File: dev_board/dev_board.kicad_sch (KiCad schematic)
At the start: 3 parts, among them P1 USB_C_Plug_USB2.0, U2 ATmega32L-8A

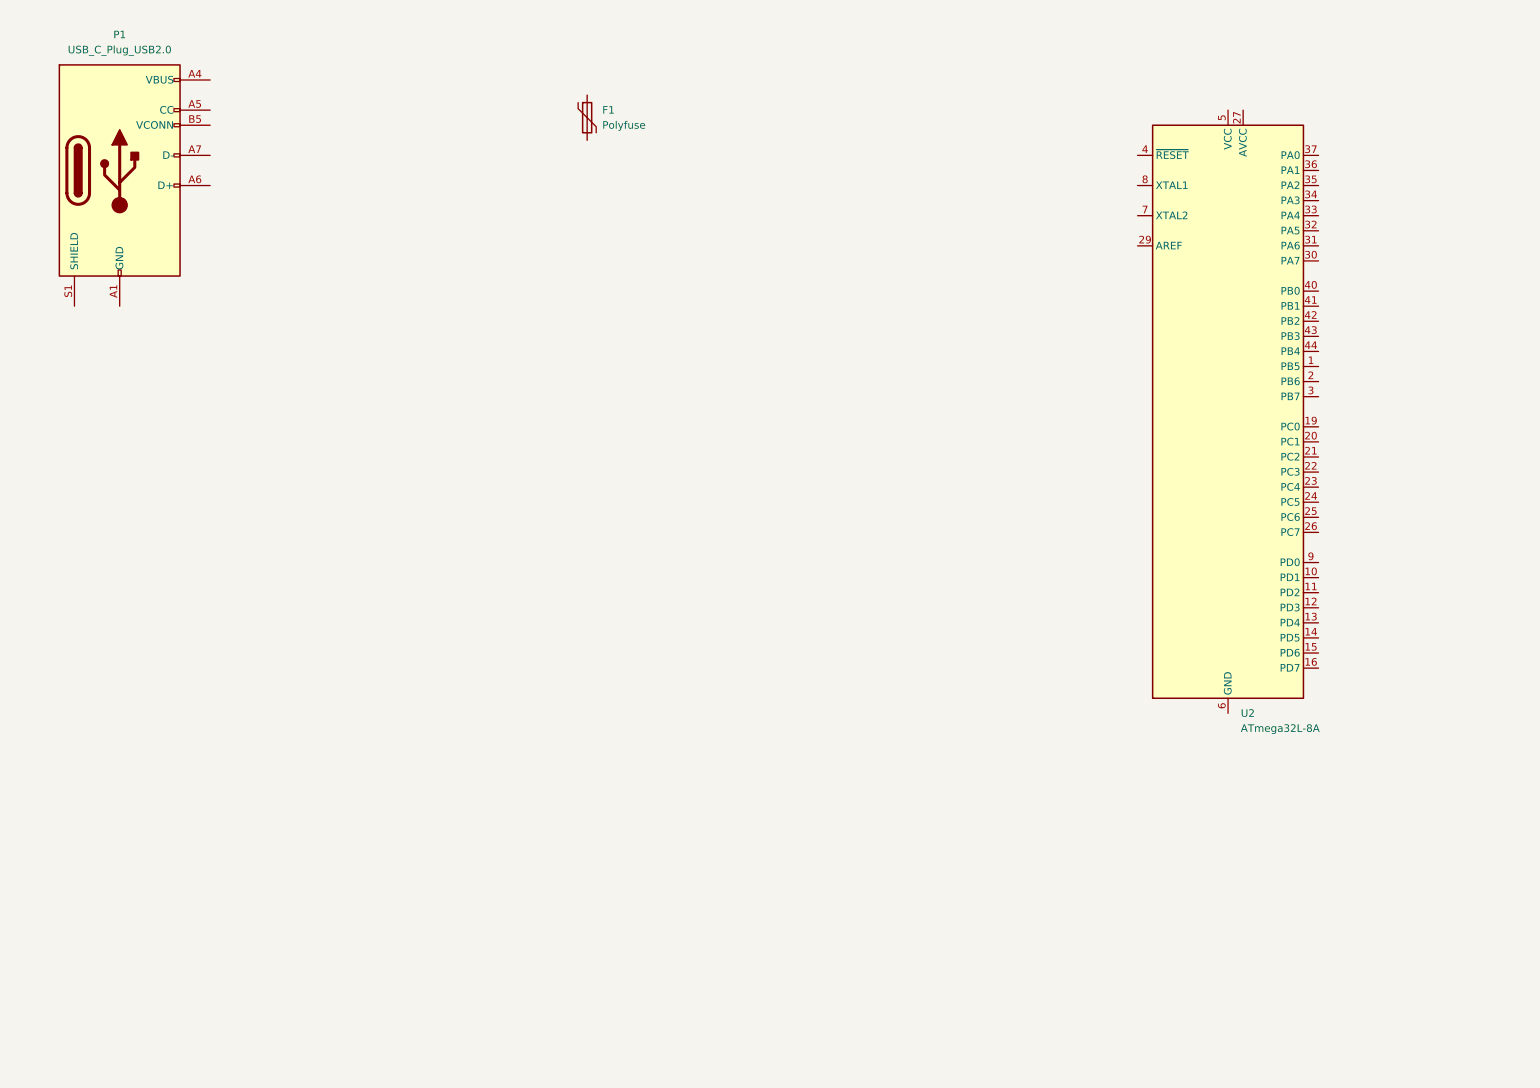
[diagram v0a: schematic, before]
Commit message: schematic autosave issue
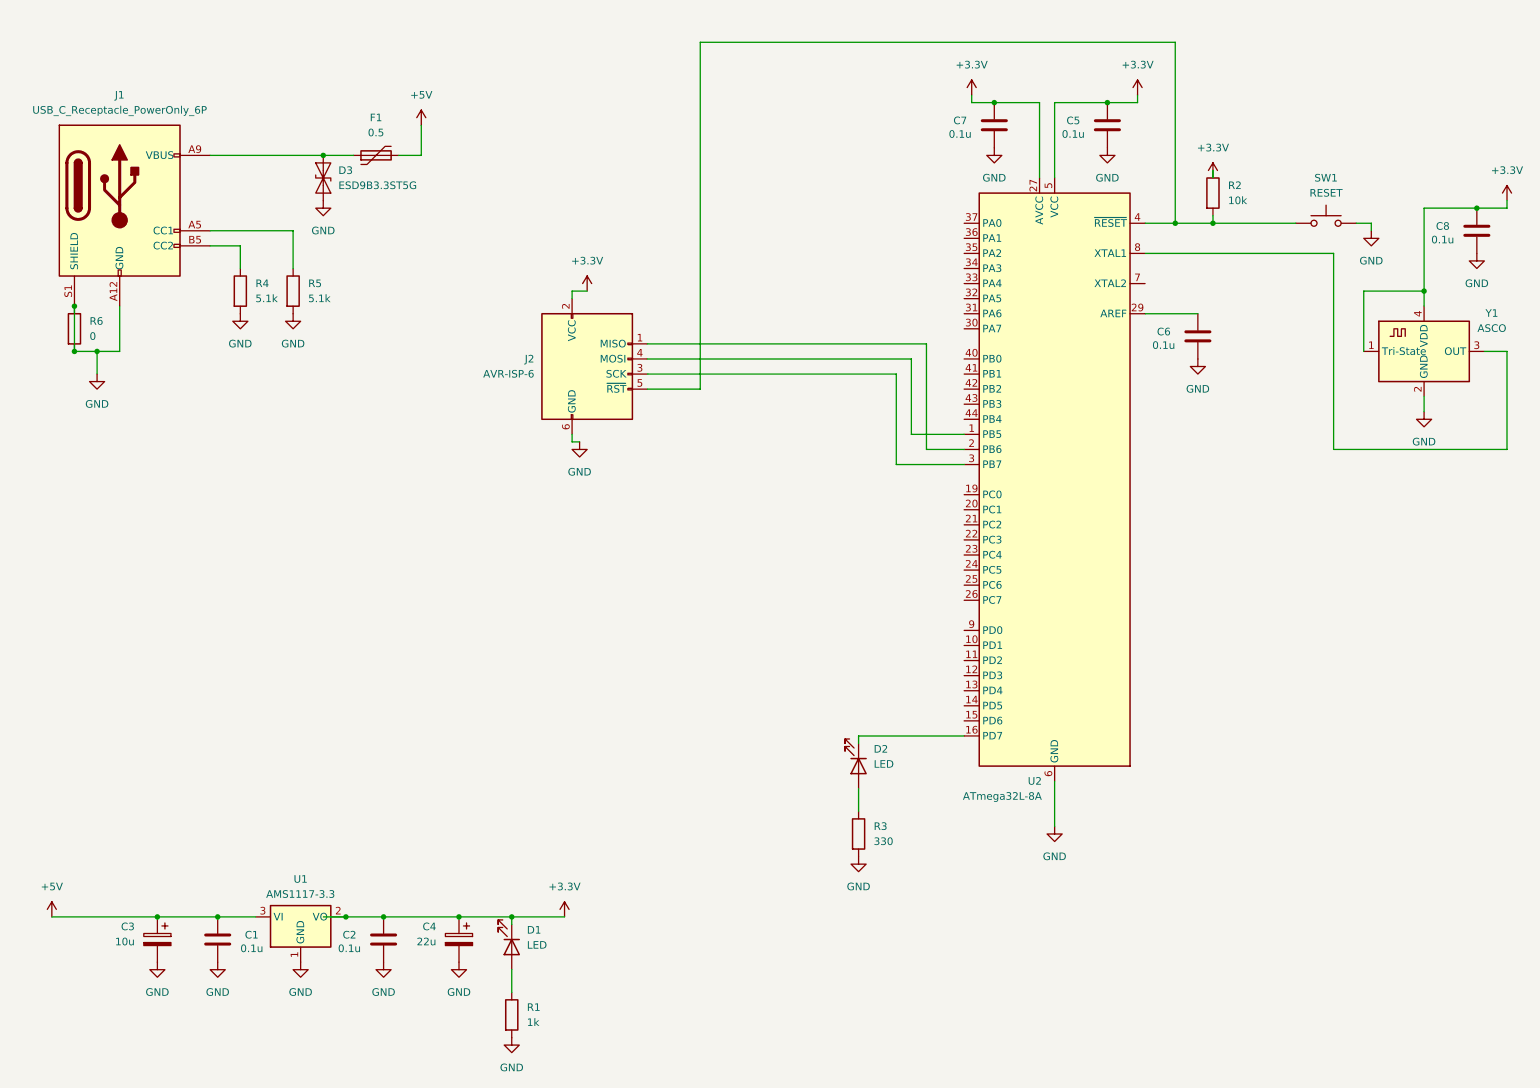
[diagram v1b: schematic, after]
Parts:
- removed P1: USB_C_Plug_USB2.0, symbol Connector:USB_C_Plug_USB2.0
- added C1, C2, C5, C6, C7, C8: 0.1u, Capacitor_SMD:C_0201_0603Metric, symbol Device:C
- added C3: 10u, Capacitor_Tantalum_SMD:CP_EIA-1608-08_AVX-J, symbol Device:C_Polarized
- added C4: 22u, Capacitor_Tantalum_SMD:CP_EIA-1608-08_AVX-J, symbol Device:C_Polarized
- added D1, D2: LED, Diode_SMD:D_0201_0603Metric, symbol Device:LED
- added D3: ESD9B3.3ST5G, Diode_SMD:D_SOD-923, symbol Diode:ESD9B3.3ST5G
- added J1: USB_C_Receptacle_PowerOnly_6P, Connector_USB:USB_C_Receptacle_Amphenol_124019772112A, symbol Connector:USB_C_Receptacle_PowerOnly_6P
- added J2: AVR-ISP-6, Package_DFN_QFN:DFN-8-1EP_2x2mm_P0.5mm_EP0.9x1.5mm, symbol Connector:AVR-ISP-6
- added R1: 1k, Resistor_SMD:R_0201_0603Metric, symbol Device:R
- added R2: 10k, Resistor_SMD:R_0201_0603Metric, symbol Device:R
- added R3: 330, Resistor_SMD:R_0201_0603Metric, symbol Device:R
- added R4, R5: 5.1k, Resistor_SMD:R_0201_0603Metric, symbol Device:R
- added R6: 0, Resistor_SMD:R_0201_0603Metric, symbol Device:R
- added SW1: RESET, Button_Switch_Keyboard:SW_Cherry_MX_1.00u_PCB, symbol Switch:SW_Push
- added U1: AMS1117-3.3, Package_TO_SOT_SMD:SOT-223-3_TabPin2, symbol Regulator_Linear:AMS1117-3.3
- added Y1: ASCO, Oscillator:Oscillator_SMD_Abracon_ASCO-4Pin_1.6x1.2mm, symbol Oscillator:ASCO
- F1: value Polyfuse -> 0.5; footprint (none) -> Fuse:Fuse_0603_1608Metric
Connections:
- net at F1.1: now also D3.1 (A1), J1.A9 (VBUS), J1.B9 (VBUS)
- net +5V: now reaches F1.2
- net +5V: now also C1.1, C3.1, U1.3 (VI)
- net at U2.1 (PB5): now also J2.4 (MOSI)
- net at U2.16 (PD7): now also D2.1 (K)
- net +3.3V: now reaches U2.17 (VCC), U2.38 (VCC), U2.5 (VCC)
- net +3.3V: now also U2.27 (AVCC), C2.1, C4.1, C5.1, C7.1, C8.1, D1.1 (K), J2.2 (VCC), R2.1, U1.2 (VO), Y1.1 (Tri-State), Y1.4 (VDD)
- net GND: now reaches U2.18 (GND), U2.28 (GND), U2.39 (GND), U2.6 (GND)
- net GND: now also C1.2, C2.2, C3.2, C4.2, C5.2, C6.2, C7.2, C8.2, D3.2 (A2), J1.A12 (GND), J1.B12 (GND), J1.S1 (SHIELD), J2.6 (GND), R1.2, R3.2, R4.2, R5.2, R6.1, R6.2, SW1.2, U1.1 (GND), Y1.2 (GND)
- net at U2.2 (PB6): now also J2.1 (MISO)
- net at U2.29 (AREF): now also C6.1
- net at U2.3 (PB7): now also J2.3 (SCK)
- net at U2.4 (~{RESET}): now also J2.5 (~{RST}), R2.2, SW1.1
- net at U2.8 (XTAL1): now also Y1.3 (OUT)
- new net: D1.2 (A), R1.1
- new net: J1.A5 (CC1), R5.1
- new net: J1.B5 (CC2), R4.1
- new net: D2.2 (A), R3.1
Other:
- moved on the sheet: F1, U2

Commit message: UART IC + test switches + extra LED's
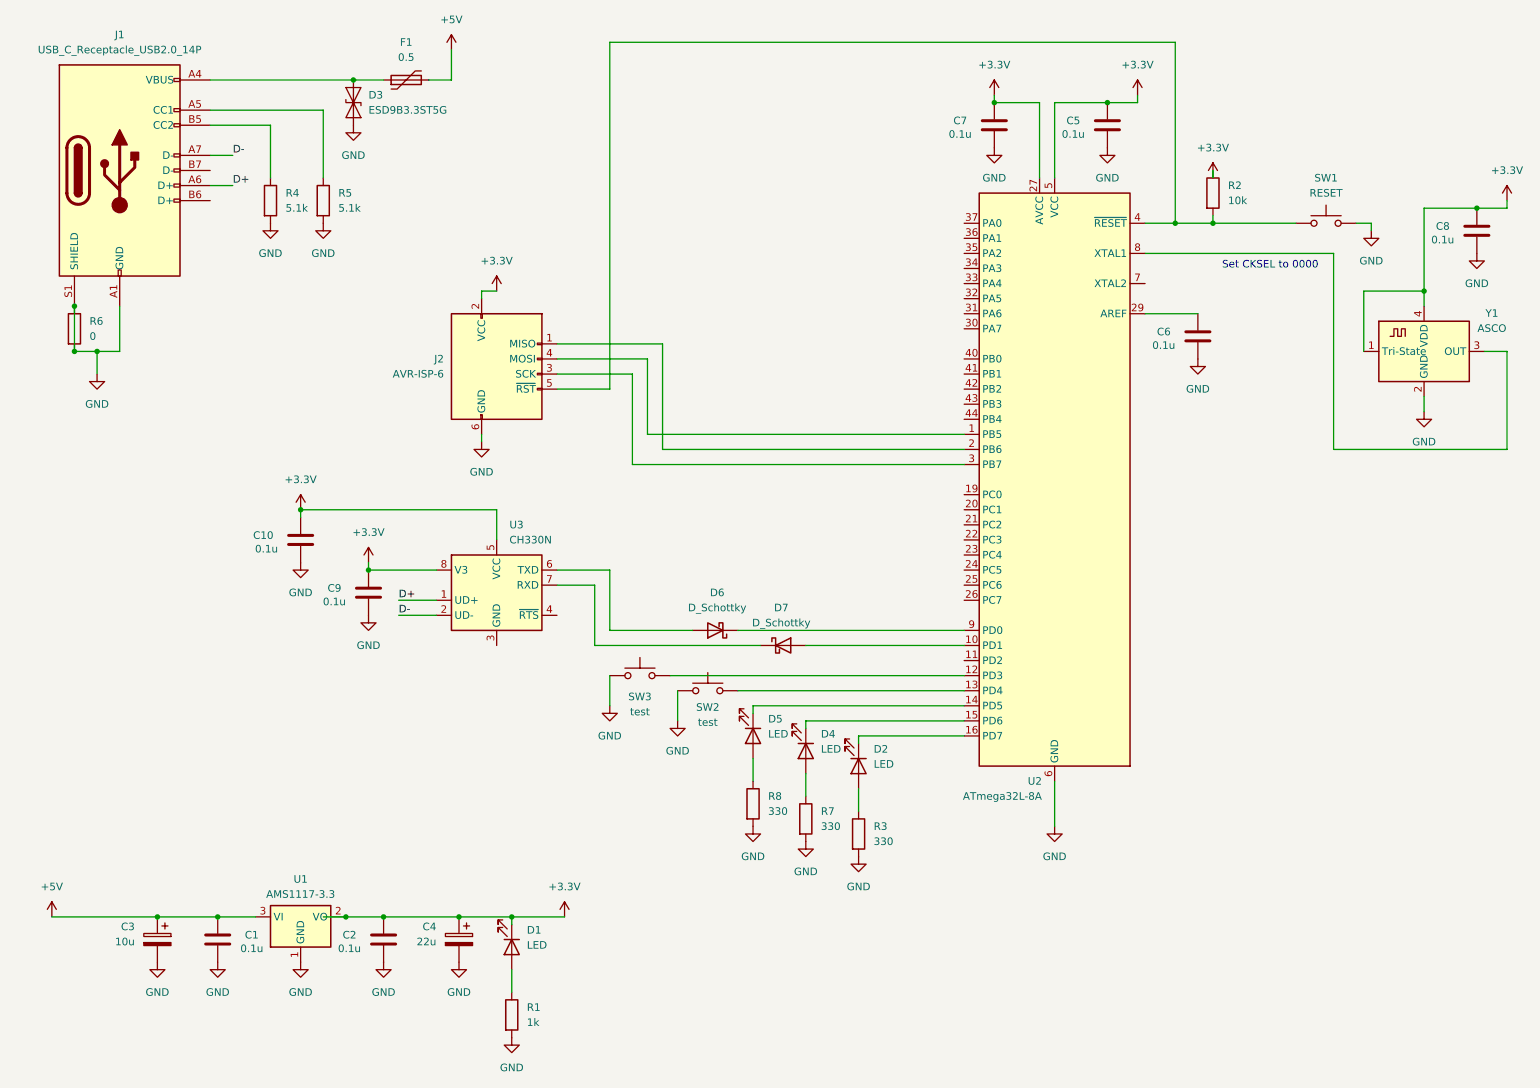
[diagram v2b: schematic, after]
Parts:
- removed J1: USB_C_Receptacle_PowerOnly_6P, Connector_USB:USB_C_Receptacle_Amphenol_124019772112A, symbol Connector:USB_C_Receptacle_PowerOnly_6P
- added C10, C9: 0.1u, Capacitor_SMD:C_0201_0603Metric, symbol Device:C
- added D4, D5: LED, Diode_SMD:D_0201_0603Metric, symbol Device:LED
- added D6, D7: D_Schottky, Diode_SMD:D_SOD-123, symbol Device:D_Schottky
- added J1: USB_C_Receptacle_USB2.0_14P, Connector_USB:USB_C_Receptacle_Amphenol_124019772112A, symbol Connector:USB_C_Receptacle_USB2.0_14P
- added R7, R8: 330, Resistor_SMD:R_0201_0603Metric, symbol Device:R
- added SW2, SW3: test, Button_Switch_Keyboard:SW_Cherry_MX_1.00u_PCB, symbol Switch:SW_Push
- added U3: CH330N, Package_SO:SOIC-8_3.9x4.9mm_P1.27mm, symbol Interface_USB:CH330N
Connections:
- net +3.3V: now also C10.1, C9.1, U3.5 (VCC), U3.8 (V3)
- net GND: now also C10.2, C9.2, J1.A1 (GND), J1.A12 (GND), J1.B1 (GND), J1.B12 (GND), J1.S1 (SHIELD), R7.2, R8.2, SW2.1, SW3.1
- net at D3.1 (A1), F1.1: now also J1.A4 (VBUS), J1.A9 (VBUS), J1.B4 (VBUS), J1.B9 (VBUS)
- net at R5.1: now also J1.A5 (CC1)
- net at R4.1: now also J1.B5 (CC2)
- net at U2.10 (PD1): now also D7.2 (A)
- net at U2.12 (PD3): now also SW3.2
- net at U2.13 (PD4): now also SW2.2
- net at U2.14 (PD5): now also D5.1 (K)
- net at U2.15 (PD6): now also D4.1 (K)
- net at U2.9 (PD0): now also D6.1 (K)
- new net: D5.2 (A), R8.1
- new net: D4.2 (A), R7.1
- new net: D6.2 (A), U3.6 (TXD)
- new net: D7.1 (K), U3.7 (RXD)
- new net D+: J1.A6 (D+), U3.1 (UD+)
- new net D-: J1.A7 (D-), U3.2 (UD-)
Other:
- note added: "Set CKSEL to 0000"
- moved on the sheet: D3, F1, J2, R4, R5

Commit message: add dev_board hierarchical sheets
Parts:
- removed C1, C10, C2, C5, C6, C7, C8, C9: 0.1u, Capacitor_SMD:C_0201_0603Metric, symbol Device:C
- removed C3: 10u, Capacitor_Tantalum_SMD:CP_EIA-1608-08_AVX-J, symbol Device:C_Polarized
- removed C4: 22u, Capacitor_Tantalum_SMD:CP_EIA-1608-08_AVX-J, symbol Device:C_Polarized
- removed D1, D2, D4, D5: LED, Diode_SMD:D_0201_0603Metric, symbol Device:LED
- removed D3: ESD9B3.3ST5G, Diode_SMD:D_SOD-923, symbol Diode:ESD9B3.3ST5G
- removed D6, D7: D_Schottky, Diode_SMD:D_SOD-123, symbol Device:D_Schottky
- removed F1: 0.5, Fuse:Fuse_0603_1608Metric, symbol Device:Polyfuse
- removed J1: USB_C_Receptacle_USB2.0_14P, Connector_USB:USB_C_Receptacle_Amphenol_124019772112A, symbol Connector:USB_C_Receptacle_USB2.0_14P
- removed J2: AVR-ISP-6, Package_DFN_QFN:DFN-8-1EP_2x2mm_P0.5mm_EP0.9x1.5mm, symbol Connector:AVR-ISP-6
- removed R1: 1k, Resistor_SMD:R_0201_0603Metric, symbol Device:R
- removed R2: 10k, Resistor_SMD:R_0201_0603Metric, symbol Device:R
- removed R3, R7, R8: 330, Resistor_SMD:R_0201_0603Metric, symbol Device:R
- removed R4, R5: 5.1k, Resistor_SMD:R_0201_0603Metric, symbol Device:R
- removed R6: 0, Resistor_SMD:R_0201_0603Metric, symbol Device:R
- removed SW1: RESET, Button_Switch_Keyboard:SW_Cherry_MX_1.00u_PCB, symbol Switch:SW_Push
- removed SW2, SW3: test, Button_Switch_Keyboard:SW_Cherry_MX_1.00u_PCB, symbol Switch:SW_Push
- removed U1: AMS1117-3.3, Package_TO_SOT_SMD:SOT-223-3_TabPin2, symbol Regulator_Linear:AMS1117-3.3
- removed U2: ATmega32L-8A, Package_QFP:TQFP-44_10x10mm_P0.8mm, symbol MCU_Microchip_ATmega:ATmega32L-8A
- removed U3: CH330N, Package_SO:SOIC-8_3.9x4.9mm_P1.27mm, symbol Interface_USB:CH330N
- removed Y1: ASCO, Oscillator:Oscillator_SMD_Abracon_ASCO-4Pin_1.6x1.2mm, symbol Oscillator:ASCO
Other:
- added sheet CONNECTORS (CONNECTORS.kicad_sch)
- added sheet MCU_MAIN (MCU_MAIN.kicad_sch)
- added sheet POWER (POWER.kicad_sch)
- note removed: "Set CKSEL to 0000"
